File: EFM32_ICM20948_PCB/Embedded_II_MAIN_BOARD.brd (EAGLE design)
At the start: 86 parts, among them IC2 EFM32HG322F64G-C-QFP48R, IC5 TPS7A0518PDBZR, Q1 20V/0.2A/8MHz/1.2Ω/1Vth, Q6 20V/0.2A/8MHz/1.2Ω/1Vth, Q8 20V/0.2A/8MHz/1.2Ω/1Vth, U3 9DoF IMU, Y2 FC-135_32.7680KA-A3, Y3 ABM3B-24.000MHZ-B2-T

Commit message: Routing main pcb
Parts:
- removed C40: 10u, microbuilder:0603
- removed JP2: ADR, SparkFun-Jumpers:SMT-JUMPER_2_NO_SILK
- added ADDR: ADR, SparkFun-Jumpers:SMT-JUMPER_2_NO_SILK
- added GND6, GND_1: TPTP20SQ, testpad:TP20SQ
- added IMU_I2C: IMU_I2C, pinhead:1X02
- added R10, R9: 10k, microbuilder:0603
- added TP1, TP18, TP19, TP2, TP20, TP7, TP8, TP9: TPTP10R, testpad:TP10R
- moved DBG_OPT 217.8 mm to (-9.65, 15.5)
- moved LORA 200.8 mm to (21.3, 3.30), turned to 90 degrees
- moved SOLAR_V 200.7 mm to (16.0, 9.40), flipped to the bottom, turned to 270 degrees
- moved R39 199.4 mm to (17.8, 13.7), flipped to the bottom, turned to 180 degrees
- moved TP16 198.1 mm to (18.5, 16.0)
- moved R29 195.3 mm to (14.0, 13.7), flipped to the bottom, turned to 180 degrees
- moved EXTRA 193.5 mm to (-25.7, 9.40), turned to 270 degrees
- moved BATT_V 192.5 mm to (16.0, 16.0), flipped to the bottom
- moved TX/RX_OPT 183.8 mm to (-21.8, -10.9), turned to 180 degrees
- moved ANALOG 183.1 mm to (21.3, 12.7), turned to 90 degrees
- moved R6 176.8 mm to (17.8, 11.7), flipped to the bottom, turned to 180 degrees
- moved R5 172.5 mm to (14.0, 11.7), flipped to the bottom, turned to 180 degrees
- moved PF0 157.2 mm to (-10.9, 12.4), flipped to the bottom, turned to 270 degrees
- moved PF1 155.0 mm to (-8.38, 12.4), flipped to the bottom, turned to 270 degrees
- moved R7 154.1 mm to (-4.06, -10.7), flipped to the bottom, turned to 270 degrees
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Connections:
- net N$1 renamed IMU_VDD_PIN
- new net !CS!_RFID: IC2.30, RFID/SPI.4
- net !CS: no longer IC2.30, RFID/SPI.4
- net AD0/SDO: now also ADDR.2; no longer JP2.2
- net DBG_!RESET: now also TP9.TP
- net GND: now also ADDR.1, GND6.TP, GND_1.TP; no longer C40.2, JP2.1
- net INT: no longer IC2.8
- net INT_VIN: now also IC2.8
- net LED: now also TP2.TP
- net LORA_EN: now also TP20.TP
- net LORA_RX: now also LORA.4, TP19.TP; no longer LORA.5
- net LORA_TX: now also LORA.5, TP18.TP; no longer LORA.4
- net PB11: no longer EXTRA.1
- net SCL: now also IMU_I2C.1, R9.1, TP8.TP
- net SDA: now also IMU_I2C.2, R10.1, TP7.TP
- net SOLAR_VOLTAGE: now also TP1.TP
- net VDD: now also R10.2, R9.2
- net V_BATT: no longer C40.1
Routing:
- net GND: track 0.00 -> 211.8 mm, vias 0 -> 11
- net VDD: track 0.00 -> 149.5 mm, vias 0 -> 6
- net DBG_!RESET: track 0.00 -> 89.5 mm, vias 0 -> 6
- net 1.8V: track 0.00 -> 71.1 mm, vias 0 -> 5
- net SDA: track 0.00 -> 59.5 mm
- net SCL: track 0.00 -> 57.6 mm, vias 0 -> 2
- net INT_VIN: track 0.00 -> 42.3 mm, vias 0 -> 4
- net PC9: track 0.00 -> 41.9 mm, vias 0 -> 3
- net PA0: track 0.00 -> 39.3 mm, vias 0 -> 1
- net PF3: track 0.00 -> 36.7 mm, vias 0 -> 2
- net PF5: track 0.00 -> 31.9 mm, vias 0 -> 2
- net PE13: track 0.00 -> 31.0 mm, vias 0 -> 1
- net IMU_VDD_PIN: track 0.00 -> 29.2 mm, vias 0 -> 1
- net PF2: track 0.00 -> 28.8 mm, vias 0 -> 1
- net DBG_SWCLK: track 0.00 -> 27.2 mm
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- added copper zone on layer 1, net GND
- added copper zone on layer 16, net GND
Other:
- board outline added: 52.8 x 35.1 mm

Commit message: main pcb lora update, bijna klaar
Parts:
- added C2, C6: 10u, rcl:C0805K
- added C3, C7: 100n, rcl:C0805K
- added C4, C5: (no value), rcl:C0603K
- added L1: WE-MK_0603_744786118, project:WE-MK_0603
- added LORA_RESET: LORA_RESET, SparkFun-Jumpers:SMT-JUMPER_2_NO_SILK
- added LORA_RX: LORA_RX, SparkFun-Jumpers:SMT-JUMPER_2_NO_SILK
- added LORA_TX: LORA_TX, SparkFun-Jumpers:SMT-JUMPER_2_NO_SILK
- added LORA_VDD: LORA_VDD, SparkFun-Jumpers:SMT-JUMPER_2_NO_SILK
- added U$2: ANTENNA868, project:CERAMIC-ANTENNA
- added U$4: RN2483, project:RN2483
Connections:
- new net N$1: C5.2, L1.2, U$2.P$1
- new net N$2: C4.2, L1.1, U$4.RFH
- new net N$6: LORA_RX.2, U$4.UART_RX
- new net N$7: LORA_TX.2, U$4.UART_TX
- new net N$8: LORA_RESET.2, U$4.RESET°
- new net VDD_LORA: C2.1, C3.1, C6.1, C7.1, LORA_VDD.2, U$4.VDD, U$4.VDD2
- net GND: now also C2.2, C3.2, C4.1, C5.1, C6.2, C7.2, U$4.GND, U$4.GND1, U$4.GND10, U$4.GND11, U$4.GND12, U$4.GND2, U$4.GND3, U$4.GND4, U$4.GND5, U$4.GND6, U$4.GND7, U$4.GND8, U$4.GND9
- net LORA_!RESET!: now also LORA_RESET.1
- net LORA_RX: now also LORA_RX.1
- net LORA_TX: now also LORA_TX.1
- net VDD: now also LORA_VDD.1
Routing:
- net GND: track 211.8 -> 354.8 mm, vias 11 -> 14
- net VDD_LORA: track 0.00 -> 26.9 mm, vias 0 -> 3
- net VDD: track 149.5 -> 172.9 mm, vias 6 -> 8
- net LORA_!RESET!: track 15.1 -> 37.6 mm, vias 1 -> 2
- net LORA_TX: track 19.0 -> 41.0 mm, vias 1 -> 2
- net LORA_RX: track 16.5 -> 35.8 mm
- net N$8: track 0.00 -> 11.0 mm, vias 0 -> 1
- net N$6: track 0.00 -> 10.5 mm, vias 0 -> 1
- net N$7: track 0.00 -> 9.88 mm, vias 0 -> 1
- net N$1: track 0.00 -> 3.36 mm
- net N$2: track 0.00 -> 3.12 mm
- removed copper zone on layer 1, net GND
- removed copper zone on layer 16, net GND
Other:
- board size 52.8 x 35.1 mm -> 76.5 x 41.4 mm

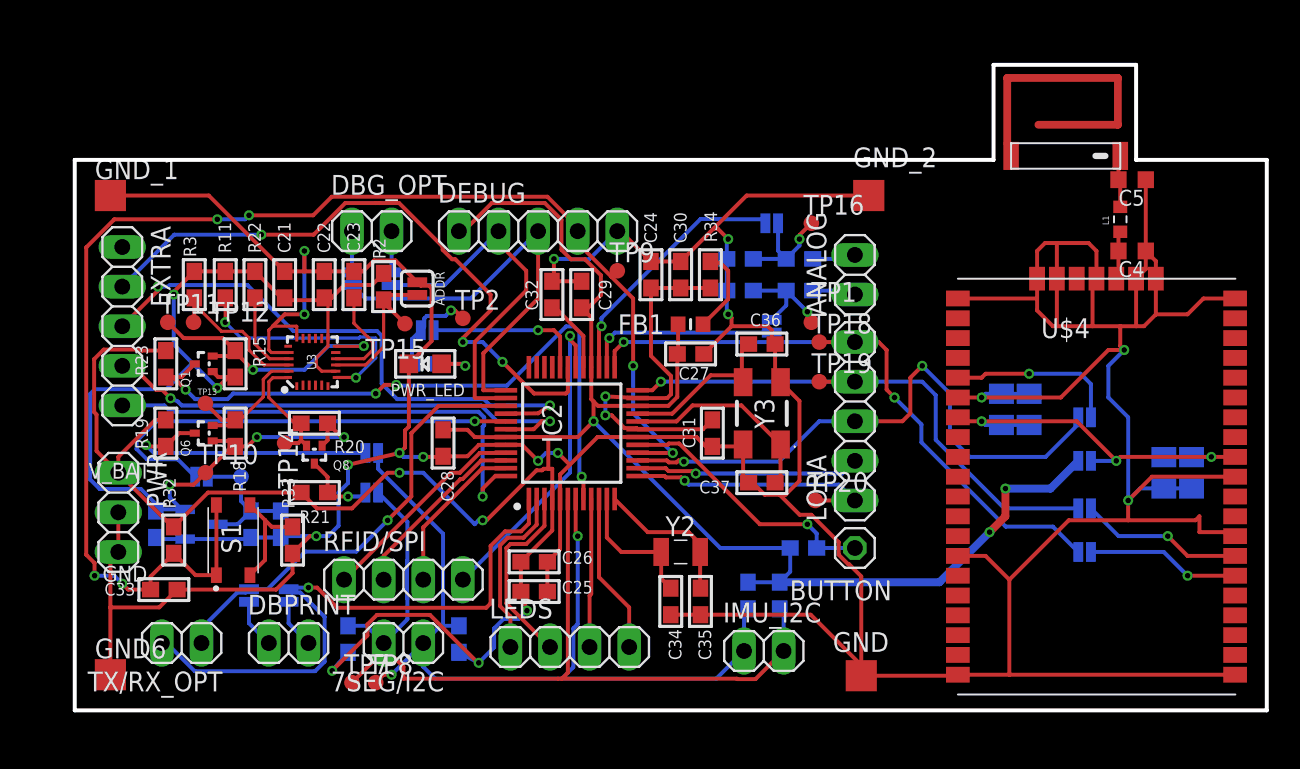
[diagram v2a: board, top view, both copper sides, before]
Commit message: finalisatie design main pcb (uC + imu + lora)
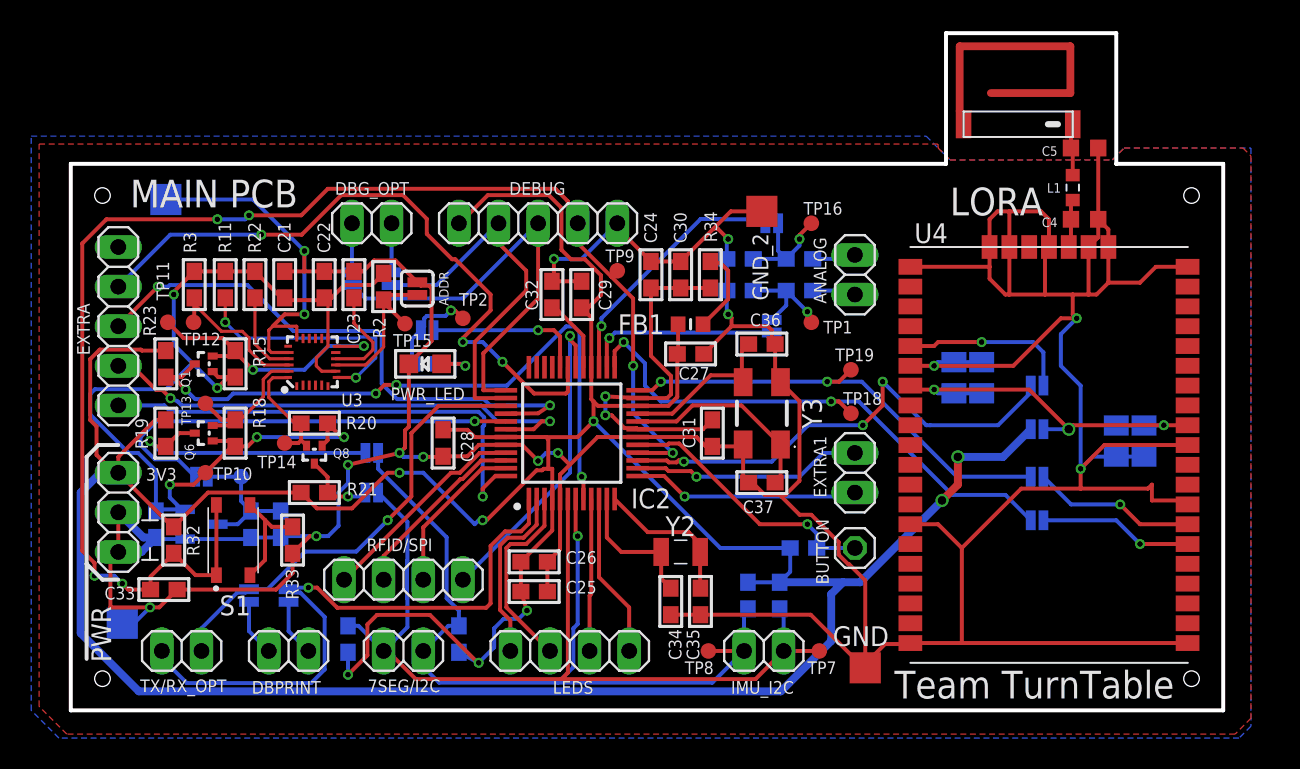
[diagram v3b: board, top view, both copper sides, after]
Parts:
- removed LORA: LORA, pinhead:1X05
- removed TP20: TPTP10R, testpad:TP10R
- removed U$4: RN2483, project:RN2483
- added EXTRA1: EXTRA, pinhead:1X02
- added U4: RN2483, project:RN2483
- moved TP7 30.0 mm to (19.1, -11.4)
- moved TP8 21.4 mm to (11.9, -11.4)
- moved GND_2 6.93 mm to (15.4, 16.8)
- moved TP18 5.00 mm to (21.1, 3.81)
- moved C2 3.66 mm to (29.5, 6.10)
- moved C3 3.66 mm to (27.7, 6.10)
- moved C4 3.66 mm to (36.1, 16.3)
- moved C5 3.66 mm to (36.1, 20.8)
- moved C6 3.66 mm to (39.9, 2.03)
- moved C7 3.66 mm to (38.1, 2.03)
- moved L1 3.66 mm to (35.3, 18.3)
- moved U$2 3.66 mm to (35.3, 22.4)
- moved LORA_RESET 3.66 mm to (33.0, 5.59)
- moved LORA_RX 3.66 mm to (33.0, -0.25)
- moved LORA_TX 3.66 mm to (33.0, -3.05)
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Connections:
- removed net LORA_EN: IC2.13, LORA.1, TP20.TP
- removed net SENSOR_EN: IC2.14, LORA.2
- new net PA8: EXTRA1.1, IC2.13
- new net PA9: EXTRA1.2, IC2.14
- net GND: now also U4.GND, U4.GND1, U4.GND10, U4.GND11, U4.GND12, U4.GND2, U4.GND3, U4.GND4, U4.GND5, U4.GND6, U4.GND7, U4.GND8, U4.GND9; no longer U$4.GND, U$4.GND1, U$4.GND10, U$4.GND11, U$4.GND12, U$4.GND2, U$4.GND3, U$4.GND4, U$4.GND5, U$4.GND6, U$4.GND7, U$4.GND8, U$4.GND9
- net LORA_!RESET!: no longer LORA.3
- net LORA_RX: no longer LORA.4
- net LORA_TX: no longer LORA.5
- net N$2: now also U4.RFH; no longer U$4.RFH
- net N$6: now also U4.UART_RX; no longer U$4.UART_RX
- net N$7: now also U4.UART_TX; no longer U$4.UART_TX
- net N$8: now also U4.RESET°; no longer U$4.RESET°
- net VDD_LORA: now also U4.VDD, U4.VDD2; no longer U$4.VDD, U$4.VDD2
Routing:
- net VDD: track 172.9 -> 238.6 mm
- net LORA_EN: track 17.1 -> 0.00 mm, vias 1 -> 0
- net PA9: track 0.00 -> 14.8 mm, vias 0 -> 1
- net PA8: track 0.00 -> 14.6 mm, vias 0 -> 1
- net SENSOR_EN: track 14.4 -> 0.00 mm, vias 1 -> 0
- net GND: track 354.8 -> 345.7 mm, vias 14 -> 15
- net LORA_!RESET!: track 37.6 -> 30.8 mm, vias 2 -> 3
- net LORA_RX: track 35.8 -> 29.8 mm, vias 1 -> 2
- net LORA_TX: track 41.0 -> 35.1 mm
- net DBG_!RESET: track 89.5 -> 91.0 mm
- net 1.8V: track 71.1 -> 69.9 mm
- net SCL: track 57.6 -> 56.5 mm, vias 2 -> 1
- net PC9: track 41.9 -> 43.0 mm
- net PA0: track 39.3 -> 40.3 mm
- net DBG_SWCLK: track 27.2 -> 27.9 mm
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- added copper zone on layer 1, net GND
- added copper zone on layer 16, net GND
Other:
- board size 76.5 x 41.4 mm -> 73.9 x 43.4 mm
- board text added: "3V3"
- board text added: "LORA"
- board text added: "MAIN PCB"
- board text added: "Team TurnTable"
- board text removed: "GND"
- board text removed: "V_BATT"

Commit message: PCB's DONE! :100:
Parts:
- EXTRA: device pinhead:1X05 -> pinhead:1X04
- moved EXTRA 1.27 mm to (-25.9, 8.13)
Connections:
- net PC9: now also EXTRA.1; no longer EXTRA.2
- net PE13: now also EXTRA.4; no longer EXTRA.5
- net PF3: now also EXTRA.2; no longer EXTRA.3
- net PF5: now also EXTRA.3; no longer EXTRA.4
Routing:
- net PF3: vias 2 -> 1
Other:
- board text added: "A0 F2"
- board text added: "A1 A2 C3 C4"
- board text added: "A9 A8 B11"
- board text added: "BATT"
- board text added: "C9 F3 F5 E13"
- board text added: "F0 F1"
- board text added: "MOSI MISO CLK !CS!"
- board text added: "RX"
- board text added: "SCL"
- board text added: "SDA"
- board text added: "SOL"
- board text added: "TX"
- board text added: "VCC I/O CLK !R! GND"
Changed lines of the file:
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@@
 <wire x1="-23.876" y1="-3.048" x2="-23.368" y2="-3.048" width="0.127" layer="25"/>
 <wire x1="-23.876" y1="-3.048" x2="-23.876" y2="-2.286" width="0.127" layer="25"/>
-<text x="-25.146" y="17.018" size="1.778" layer="25">MAIN PCB</text>
+<text x="-25.146" y="16.764" size="1.778" layer="25">MAIN PCB</text>
 <circle x="32.713165625" y="20.785025" radius="0.254" width="0.254" layer="26"/>
 <wire x1="31.552890625" y1="21.946190625" x2="33.838890625" y2="21.946190625" width="0.254" layer="26" curve="-104.250033"/>
 <wire x1="30.123709375" y1="23.46288125" x2="35.203709375" y2="23.46288125" width="0.254" layer="26" curve="-79.611142"/>
 <wire x1="28.702" y1="24.892" x2="36.576" y2="24.892" width="0.254" layer="26" curve="-84.714909"/>
+<text x="-17.018" y="-9.652" size="0.8128" layer="25">TX</text>
+<text x="-14.478" y="-9.652" size="0.8128" layer="25">RX</text>
+<text x="-10.16" y="-9.652" size="0.8128" layer="25">SDA</text>
+<text x="-7.366" y="-9.652" size="0.8128" layer="25">SCL</text>
+<text x="13.208" y="-9.652" size="0.8128" layer="25">SCL</text>
+<text x="15.748" y="-9.652" size="0.8128" layer="25">SDA</text>
+<text x="23.876" y="12.954" size="0.8128" layer="25" rot="R90">BATT</text>
+<text x="23.876" y="10.16" size="0.8128" layer="25" rot="R90">SOL</text>
+<text x="-26.67" y="13.462" size="0.6096" layer="25">C9
+F3
+F5
+E13</text>
+<text x="-6.096" y="13.716" size="0.6096" layer="25" rot="R90">F0
+F1</text>
+<text x="8.128" y="17.78" size="0.6096" layer="25" rot="R90">VCC
+I/O
+CLK
+!R!
+GND</text>
+<text x="20.828" y="-9.144" size="0.6096" layer="25">A9
+A8
+B11</text>
+<text x="7.112" y="-9.398" size="0.6096" layer="25" rot="R90">A1
+A2
+C3
+C4</text>
+<text x="-21.082" y="-9.906" size="0.6096" layer="25" rot="R90">A0
+F2</text>
+<text x="-3.048" y="-3.81" size="0.6096" layer="25" rot="R90">MOSI
+MISO
+CLK
+!CS!</text>
 </plain>
 <attributes>
@@
 <attribute name="VALUE" x="17.145" y="9.398" size="0.6096" layer="28" font="vector" ratio="20" rot="MR270" align="top-center"/>
 </element>
-<element name="EXTRA" library="pinhead" library_urn="urn:adsk.eagle:library:325" package="1X05" package3d_urn="urn:adsk.eagle:package:22469/2" value="EXTRA" x="-25.908" y="9.398" smashed="yes" rot="R270">
-<attribute name="NAME" x="-27.7368" y="7.5438" size="0.8128" layer="25" ratio="10" rot="R90"/>
-<attribute name="VALUE" x="-29.083" y="15.748" size="1.27" layer="27" rot="R270"/>
-</element>
 <element name="TX/RX_OPT" library="pinhead" library_urn="urn:adsk.eagle:library:325" package="1X02" package3d_urn="urn:adsk.eagle:package:22435/2" value="TX/RX_OPT" x="-21.844" y="-11.43" smashed="yes" rot="R180">
 <attribute name="NAME" x="-18.9738" y="-13.2588" size="0.8128" layer="25" ratio="10" rot="R180"/>
@@
 </element>
 <element name="DBG_OPT" library="pinhead" library_urn="urn:adsk.eagle:library:325" package="1X02" package3d_urn="urn:adsk.eagle:package:22435/2" value="DBG_OPT" x="-9.652" y="16.002" smashed="yes">
-<attribute name="NAME" x="-12.0142" y="17.8308" size="0.8128" layer="25" ratio="10"/>
+<attribute name="NAME" x="-12.2682" y="17.8308" size="0.8128" layer="25" ratio="10"/>
 <attribute name="VALUE" x="-12.192" y="12.827" size="1.27" layer="27"/>
 </element>
@@
 </element>
 <element name="TP9" library="testpad" library_urn="urn:adsk.eagle:library:385" package="TP10R" package3d_urn="urn:adsk.eagle:package:27959/1" value="TPTP10R" x="6.096" y="12.954" smashed="yes">
-<attribute name="NAME" x="5.3419" y="13.5039" size="0.8128" layer="25"/>
+<attribute name="NAME" x="7.0701" y="10.4219" size="0.8128" layer="25" rot="R90"/>
 <attribute name="TP_SIGNAL_NAME" value="" x="6.096" y="11.049" size="1" layer="37"/>
 <attribute name="VALUE" x="5.715" y="12.446" size="0.0254" layer="27"/>
@@
 <attribute name="NAME" x="19.5072" y="-1.6002" size="0.8128" layer="25" ratio="10" rot="R90"/>
 <attribute name="VALUE" x="24.511" y="-2.54" size="1.27" layer="27" rot="R90"/>
+</element>
+<element name="EXTRA" library="pinhead" library_urn="urn:adsk.eagle:library:325" package="1X04" package3d_urn="urn:adsk.eagle:package:22407/2" value="EXTRA" x="-25.908" y="8.128" smashed="yes" rot="R270">
+<attribute name="NAME" x="-28.3972" y="9.9822" size="0.8128" layer="25" ratio="10" rot="R270"/>
+<attribute name="VALUE" x="-29.083" y="13.208" size="1.27" layer="27" rot="R270"/>
 </element>
 </elements>
@@
 <wire x1="-22.86" y1="6.135" x2="-21.855" y2="6.135" width="0.254" layer="1"/>
 <wire x1="-21.855" y1="6.135" x2="-21.005" y2="6.985" width="0.254" layer="1"/>
-<wire x1="3.925" y1="-1.685" x2="3.925" y2="-0.369" width="0.254" layer="1"/>
-<wire x1="3.925" y1="-0.369" x2="3.81" y2="-0.254" width="0.254" layer="1"/>
-<via x="3.81" y="-0.254" extent="1-16" drill="0.35"/>
+<wire x1="3.925" y1="-1.685" x2="3.925" y2="0.115" width="0.254" layer="1"/>
+<wire x1="3.925" y1="0.115" x2="4.318" y2="0.508" width="0.254" layer="1"/>
+<via x="4.318" y="0.508" extent="1-16" drill="0.35"/>
 <via x="-21.59" y="5.334" extent="1-16" drill="0.35"/>
 <wire x1="3.6695125" y1="9.0305" x2="3.31405625" y2="9.38595625" width="0.254" layer="16"/>
 <wire x1="3.31405625" y1="9.38595625" x2="2.81135625" y2="9.38595625" width="0.254" layer="16"/>
-<wire x1="3.81" y1="-0.254" x2="3.6695125" y2="-0.1135125" width="0.254" layer="16"/>
+<wire x1="4.318" y1="0.508" x2="3.6695125" y2="1.1564875" width="0.254" layer="16"/>
 <wire x1="2.81135625" y1="9.38595625" x2="-0.9866" y2="5.588" width="0.254" layer="16"/>
-<wire x1="3.6695125" y1="-0.1135125" x2="3.6695125" y2="9.0305" width="0.254" layer="16"/>
+<wire x1="3.6695125" y1="1.1564875" x2="3.6695125" y2="9.0305" width="0.254" layer="16"/>
 <wire x1="-21.59" y1="5.334" x2="-22.391" y2="6.135" width="0.254" layer="1"/>
 <wire x1="-22.86" y1="6.135" x2="-22.391" y2="6.135" width="0.254" layer="1"/>
@@
 <signal name="PE13">
 <contactref element="IC2" pad="48"/>
-<contactref element="EXTRA" pad="5"/>
 <via x="-2.54" y="-1.524" extent="1-16" drill="0.35"/>
-<wire x1="-25.908" y1="4.318" x2="-22.95615" y2="4.318" width="0.254" layer="16"/>
 <wire x1="-2.79665" y1="3.9088" x2="-2.4412" y2="3.55335" width="0.254" layer="16"/>
 <wire x1="-2.4412" y1="3.55335" x2="-2.4412" y2="3.05065" width="0.254" layer="16"/>
 <wire x1="-2.4412" y1="3.05065" x2="-2.54" y2="2.95185" width="0.254" layer="16"/>
 <wire x1="-2.54" y1="2.95185" x2="-2.54" y2="-1.524" width="0.254" layer="16"/>
-<wire x1="-22.95615" y1="4.318" x2="-22.54695" y2="3.9088" width="0.254" layer="16"/>
-<wire x1="-22.54695" y1="3.9088" x2="-2.79665" y2="3.9088" width="0.254" layer="16"/>
+<wire x1="-25.59495" y1="3.9088" x2="-25.908" y2="4.22185" width="0.254" layer="16"/>
+<wire x1="-25.908" y1="4.318" x2="-25.908" y2="4.22185" width="0.254" layer="16"/>
+<wire x1="-25.59495" y1="3.9088" x2="-2.79665" y2="3.9088" width="0.254" layer="16"/>
 <wire x1="-1.05" y1="-0.21" x2="-1.734" y2="-0.21" width="0.254" layer="1"/>
 <wire x1="-2.54" y1="-1.016" x2="-2.54" y2="-1.524" width="0.254" layer="1"/>
 <wire x1="-1.734" y1="-0.21" x2="-2.54" y2="-1.016" width="0.254" layer="1"/>
+<contactref element="EXTRA" pad="4"/>
 </signal>
 <signal name="PC9">
 <contactref element="IC2" pad="31"/>
-<contactref element="EXTRA" pad="2"/>
 <wire x1="2.925" y1="6.765" x2="2.925" y2="5.211" width="0.254" layer="1"/>
 <wire x1="2.925" y1="5.211" x2="2.794" y2="5.08" width="0.254" layer="1"/>
@@
 <wire x1="-11.6073625" y1="17.8054" x2="-14.1441875" y2="15.268575" width="0.254" layer="1"/>
 <wire x1="-16.735425" y1="15.268575" x2="-22.577425" y2="15.268575" width="0.254" layer="16"/>
+<contactref element="EXTRA" pad="1"/>
 <wire x1="-22.577425" y1="15.268575" x2="-25.908" y2="11.938" width="0.254" layer="16"/>
 </signal>
@@
 <signal name="PF3">
 <contactref element="IC2" pad="40"/>
-<contactref element="EXTRA" pad="3"/>
-<wire x1="-25.908" y1="9.398" x2="-23.368" y2="11.938" width="0.254" layer="1"/>
-<via x="-23.368" y="11.938" extent="1-16" drill="0.35"/>
 <wire x1="-9.31358125" y1="9.0904" x2="-9.017" y2="8.79381875" width="0.254" layer="16"/>
 <via x="1.778" y="4.318" extent="1-16" drill="0.35"/>
@@
 <wire x1="-14.6784" y1="9.0904" x2="-9.31358125" y2="9.0904" width="0.254" layer="16"/>
 <wire x1="-17.6248" y1="12.0368" x2="-14.6784" y2="9.0904" width="0.254" layer="16"/>
+<contactref element="EXTRA" pad="2"/>
+<wire x1="-25.908" y1="9.398" x2="-23.368" y2="11.938" width="0.254" layer="16"/>
 </signal>
 <signal name="PF5">
 <contactref element="IC2" pad="42"/>
-<contactref element="EXTRA" pad="4"/>
 <via x="1.778" y="3.302" extent="1-16" drill="0.35"/>
 <wire x1="1.24813125" y1="3.302" x2="1.778" y2="3.302" width="0.254" layer="1"/>
@@
 <wire x1="-22.557925" y1="4.777925" x2="-23.0856" y2="5.3056" width="0.254" layer="1"/>
 <wire x1="-23.0856" y1="5.3056" x2="-23.47573125" y2="5.3056" width="0.254" layer="1"/>
-<wire x1="-25.02813125" y1="6.858" x2="-25.908" y2="6.858" width="0.254" layer="1"/>
-<wire x1="-23.47573125" y1="5.3056" x2="-25.02813125" y2="6.858" width="0.254" layer="1"/>
+<wire x1="-23.47573125" y1="5.3056" x2="-24.579065625" y2="6.408934375" width="0.254" layer="1"/>
 <wire x1="-22.098" y1="4.572" x2="-21.8412" y2="4.3152" width="0.254" layer="16"/>
 <wire x1="-21.8412" y1="4.3152" x2="-2.6283125" y2="4.3152" width="0.254" layer="16"/>
+<contactref element="EXTRA" pad="3"/>
+<wire x1="-24.579065625" y1="6.408934375" x2="-25.458934375" y2="6.408934375" width="0.254" layer="1"/>
+<wire x1="-25.458934375" y1="6.408934375" x2="-25.908" y2="6.858" width="0.254" layer="1"/>
 </signal>
 <signal name="DBPRINT_TX">
@@
 </drawing>
 <compatibility>
+<note version="6.3" minversion="6.2.2" severity="warning">
+Since Version 6.2.2 text objects can contain more than one line,
+which will not be processed correctly with this version.
+</note>
 <note version="8.2" severity="warning">
 Since Version 8.2, EAGLE supports online libraries. The ids
